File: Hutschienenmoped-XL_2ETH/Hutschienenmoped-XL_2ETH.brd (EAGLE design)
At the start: 166.3 x 101.8 mm, 118 parts, among them J1 638207222005, J13 638207222005, J15 638207222008, J2 645004114822, J3 61302211821, J4 61300421121, J6 61302211821, J7 638207222005, J8 638207222007, U1 ESP32-S3-DEVKITC-1-N8R2, U4 TLE9250VSJ

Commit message: gitflow-feature-stash: ETH
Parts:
- added J10: 61300811821, Wurth_Connectors_WR-PHD:61300811821
- added J11: 61300611821, Wurth_Connectors_WR-PHD:61300611821
- added J12: 61300615721, Wurth_Connectors_WR-PHD:61300615721
- added J14: 61300815721, Wurth_Connectors_WR-PHD:61300815721
- added MP1, MP2, MP3, MP4: M3 x 2.5mm, Wurth_Assembly_WA-SMSI:WA-SMSI_9774025360
- renumbered J3 to ESP32-J1, J6 to ESP32-J3
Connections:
- removed net IX00: U1.J1_20
- removed net IX06: U1.J1_8
- removed net MB_UART_RTS1: U1.J1_16
- removed net MB_UART_RXD1: U1.J1_12
- removed net MB_UART_RXD2: U1.J1_17
- removed net QX06: U1.J3_16
- removed net QX07: U1.J3_10
- net +3V3: now also ESP32-J1.1, ESP32-J1.2
- net +5V: now also ESP32-J1.21
- net BOOT: now also ESP32-J3.14
- net CAN1_RXD: now also ESP32-J1.5
- net CAN1_TXD: now also ESP32-J1.4
- net CI1: now also ESP32-J1.19
- net CI2: now also ESP32-J1.18
- net CI3: now also ESP32-J1.15
- net CI4: now also ESP32-J1.13
- net CI5: now also ESP32-J1.11
- net CI6: now also ESP32-J1.10
- net CI7: now also ESP32-J1.7
- net CI8: now also ESP32-J1.6
- net ECU_GND: now also ESP32-J1.22, ESP32-J3.1, ESP32-J3.21, ESP32-J3.22
- net Q1C: now also ESP32-J3.18
- net Q2C: now also ESP32-J3.17
- net Q3C: now also ESP32-J3.9
- net Q4C: now also ESP32-J3.8
- net Q5C: now also ESP32-J3.7
- net Q6C: now also ESP32-J3.6
- net Q7C: now also ESP32-J3.4
- net Q8C: now also ESP32-J3.5
- net RESET: now also ESP32-J1.3

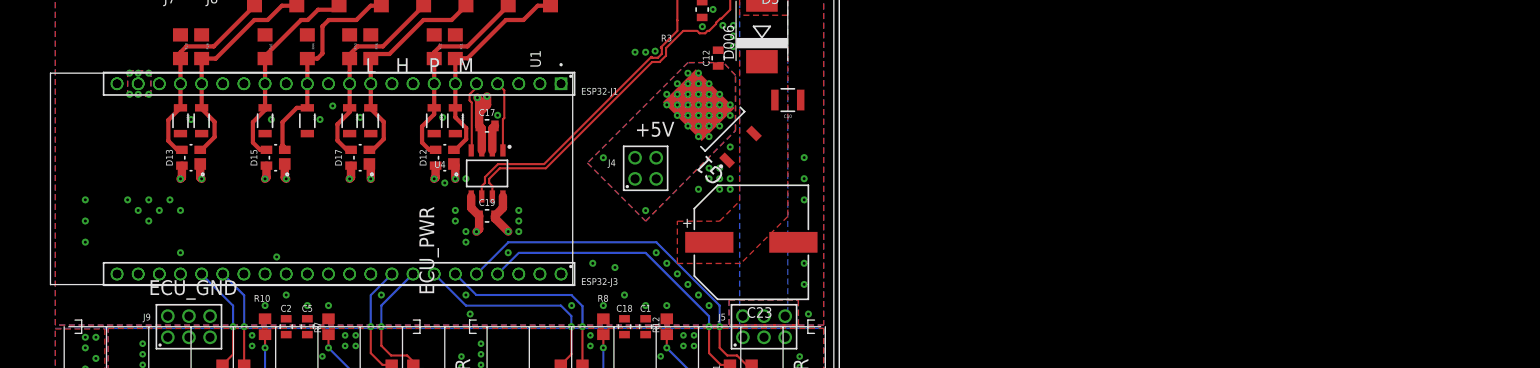
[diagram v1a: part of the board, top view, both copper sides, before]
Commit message: Update component position in board layout.
Adjusted coordinates for a component on the board to new location.
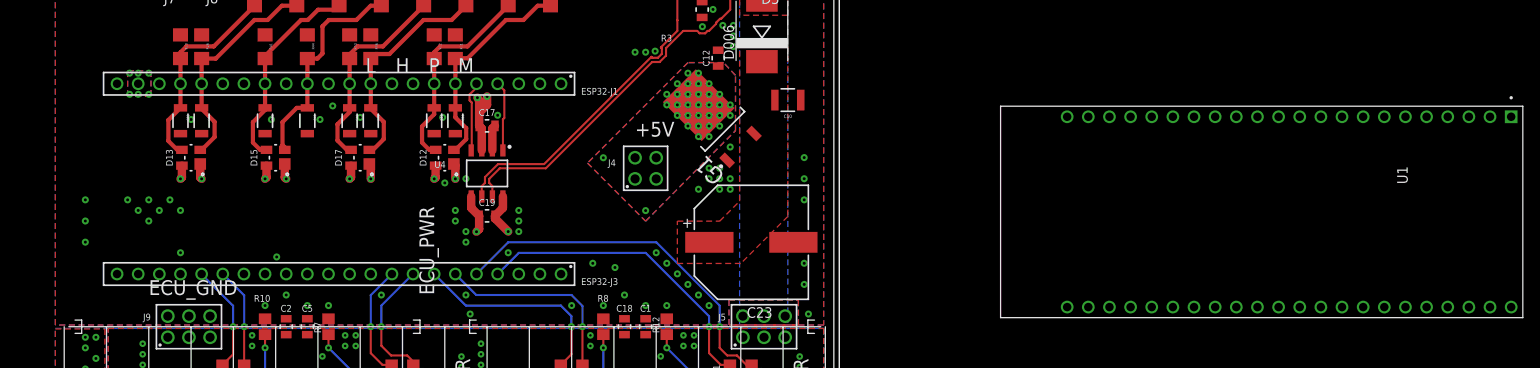
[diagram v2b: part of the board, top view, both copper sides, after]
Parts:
- moved U1 114.2 mm to (146.4, 54.5)
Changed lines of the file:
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@@
 <attribute name="VIEWING-ANGLE" value="120°" x="38.735" y="17.8" size="1.778" layer="27" display="off"/>
 </element>
-<element name="U1" library="ESP32-S3-DEVKITC-1-N8R2" library_urn="urn:adsk.eagle:library:34329045" package="XCVR_ESP32-S3-DEVKITC-1-N8R2" package3d_urn="urn:adsk.eagle:package:34329048/2" value="ESP32-S3-DEVKITC-1-N8R2" x="32.26" y="58.42" smashed="yes" rot="R270">
-<attribute name="AVAILABILITY" value="In Stock" x="102.11" y="86.36" size="1.778" layer="27" rot="R270" display="off"/>
-<attribute name="DESCRIPTION" value=" WiFi Development Tools - 802.11 (Engineering Samples Only) ESP32-S3 General-Purpose Development Board, ESP32-S3-WROOM-1-N8R2, with Pin Header " x="102.11" y="86.36" size="1.778" layer="27" rot="R270" display="off"/>
-<attribute name="MF" value="Espressif Systems" x="102.11" y="86.36" size="1.778" layer="27" rot="R270" display="off"/>
-<attribute name="MP" value="ESP32-S3-DEVKITC-1-N8R2" x="102.11" y="86.36" size="1.778" layer="27" rot="R270" display="off"/>
-<attribute name="NAME" x="58.53" y="73.91" size="1.27" layer="25" rot="R270"/>
-<attribute name="PACKAGE" value="None" x="102.11" y="86.36" size="1.778" layer="27" rot="R270" display="off"/>
-<attribute name="PRICE" value="None" x="102.11" y="86.36" size="1.778" layer="27" rot="R270" display="off"/>
-<attribute name="PURCHASE-URL" value="https://pricing.snapeda.com/search/part/ESP32-S3-DEVKITC-1-N8R2/?ref=eda" x="102.11" y="86.36" size="1.778" layer="27" rot="R270" display="off"/>
-<attribute name="VALUE" x="-0.36" y="71.37" size="1.27" layer="27" rot="R270" align="top-left"/>
+<element name="U1" library="ESP32-S3-DEVKITC-1-N8R2" library_urn="urn:adsk.eagle:library:34329045" package="XCVR_ESP32-S3-DEVKITC-1-N8R2" package3d_urn="urn:adsk.eagle:package:34329048/2" value="ESP32-S3-DEVKITC-1-N8R2" x="146.4" y="54.45" smashed="yes" rot="R270">
+<attribute name="AVAILABILITY" value="In Stock" x="206.25" y="72.39" size="1.778" layer="27" rot="R270" display="off"/>
+<attribute name="DESCRIPTION" value=" WiFi Development Tools - 802.11 (Engineering Samples Only) ESP32-S3 General-Purpose Development Board, ESP32-S3-WROOM-1-N8R2, with Pin Header " x="206.25" y="72.39" size="1.778" layer="27" rot="R270" display="off"/>
+<attribute name="MF" value="Espressif Systems" x="206.25" y="72.39" size="1.778" layer="27" rot="R270" display="off"/>
+<attribute name="MP" value="ESP32-S3-DEVKITC-1-N8R2" x="206.25" y="72.39" size="1.778" layer="27" rot="R270" display="off"/>
+<attribute name="NAME" x="162.67" y="59.94" size="1.27" layer="25" rot="R270"/>
+<attribute name="PACKAGE" value="None" x="206.25" y="72.39" size="1.778" layer="27" rot="R270" display="off"/>
+<attribute name="PRICE" value="None" x="206.25" y="72.39" size="1.778" layer="27" rot="R270" display="off"/>
+<attribute name="PURCHASE-URL" value="https://pricing.snapeda.com/search/part/ESP32-S3-DEVKITC-1-N8R2/?ref=eda" x="206.25" y="72.39" size="1.778" layer="27" rot="R270" display="off"/>
+<attribute name="VALUE" x="103.78" y="57.4" size="1.27" layer="27" rot="R270" align="top-left"/>
 </element>
 <element name="U5" library="BTS7030-2EPA" package="SOP65P600X115-15N-V" value="" x="63.5" y="29.23" smashed="yes" rot="R270">

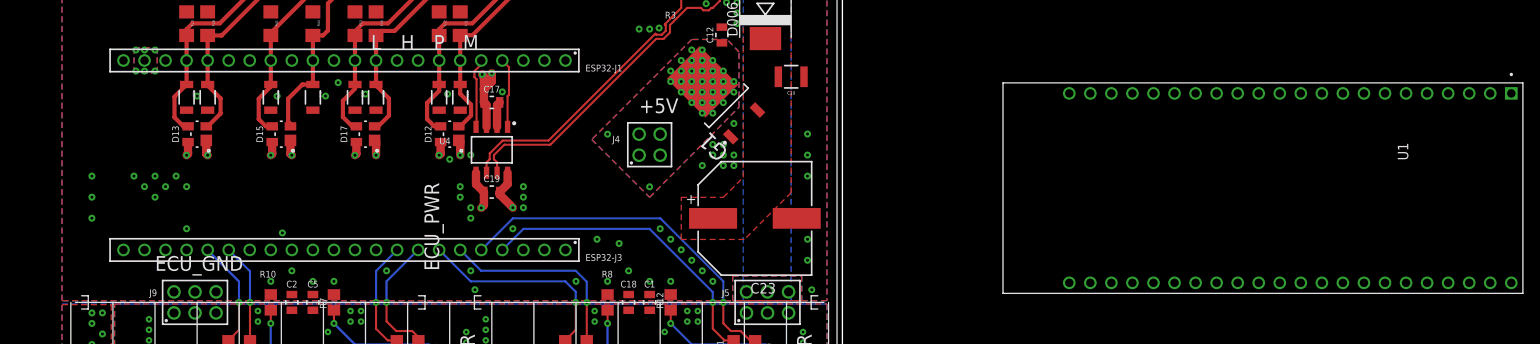
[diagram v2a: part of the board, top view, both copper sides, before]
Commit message: Add new wire connections and curves in the board design.
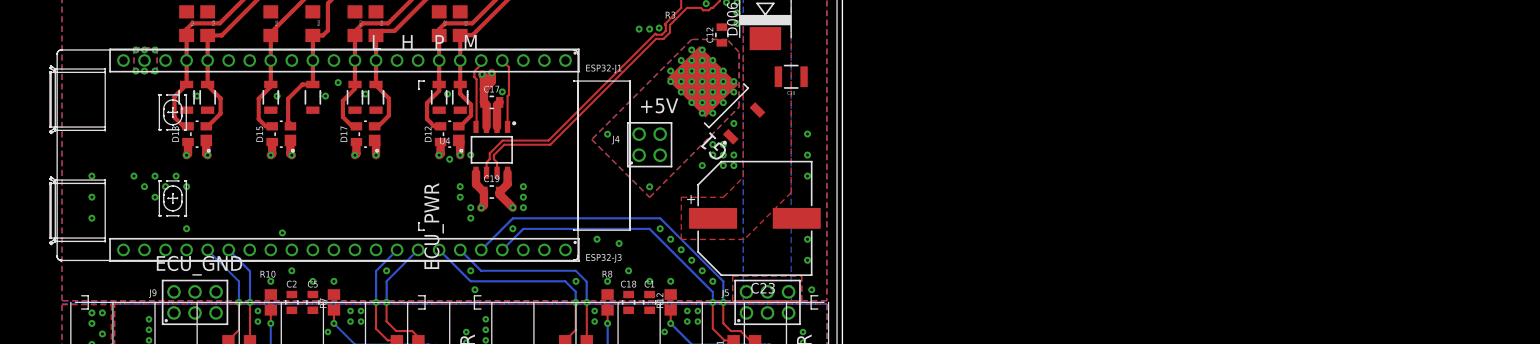
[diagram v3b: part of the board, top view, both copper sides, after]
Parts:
- removed U1: ESP32-S3-DEVKITC-1-N8R2, ESP32-S3-DEVKITC-1-N8R2:XCVR_ESP32-S3-DEVKITC-1-N8R2
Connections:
- net +3V3: no longer U1.J1_1, U1.J1_2
- net +5V: no longer U1.J1_21
- net BOOT: no longer U1.J3_14
- net CAN1_RXD: no longer U1.J1_5
- net CAN1_TXD: no longer U1.J1_4
- net CI1: no longer U1.J1_19
- net CI2: no longer U1.J1_18
- net CI3: no longer U1.J1_15
- net CI4: no longer U1.J1_13
- net CI5: no longer U1.J1_11
- net CI6: no longer U1.J1_10
- net CI7: no longer U1.J1_7
- net CI8: no longer U1.J1_6
- net ECU_GND: no longer U1.J1_22, U1.J3_1, U1.J3_21, U1.J3_22
- net Q1C: no longer U1.J3_18
- net Q2C: no longer U1.J3_17
- net Q3C: no longer U1.J3_9
- net Q4C: no longer U1.J3_8
- net Q5C: no longer U1.J3_7
- net Q6C: no longer U1.J3_6
- net Q7C: no longer U1.J3_4
- net Q8C: no longer U1.J3_5
- net RESET: no longer U1.J1_3
